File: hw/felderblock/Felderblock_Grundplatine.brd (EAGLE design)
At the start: 100 x 78 mm, 52 parts, among them IC2 LM2936, IC3 ULN2803, IC4 MCP2300X/P, J1 RJ11, J2 RJ11, M1 ARDUINO-NANO-3.0, T2 BC337, X1 TASTENSPERRE1, X2 TASTENSPERRE2, X3 SCHLUESSELSPERRE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

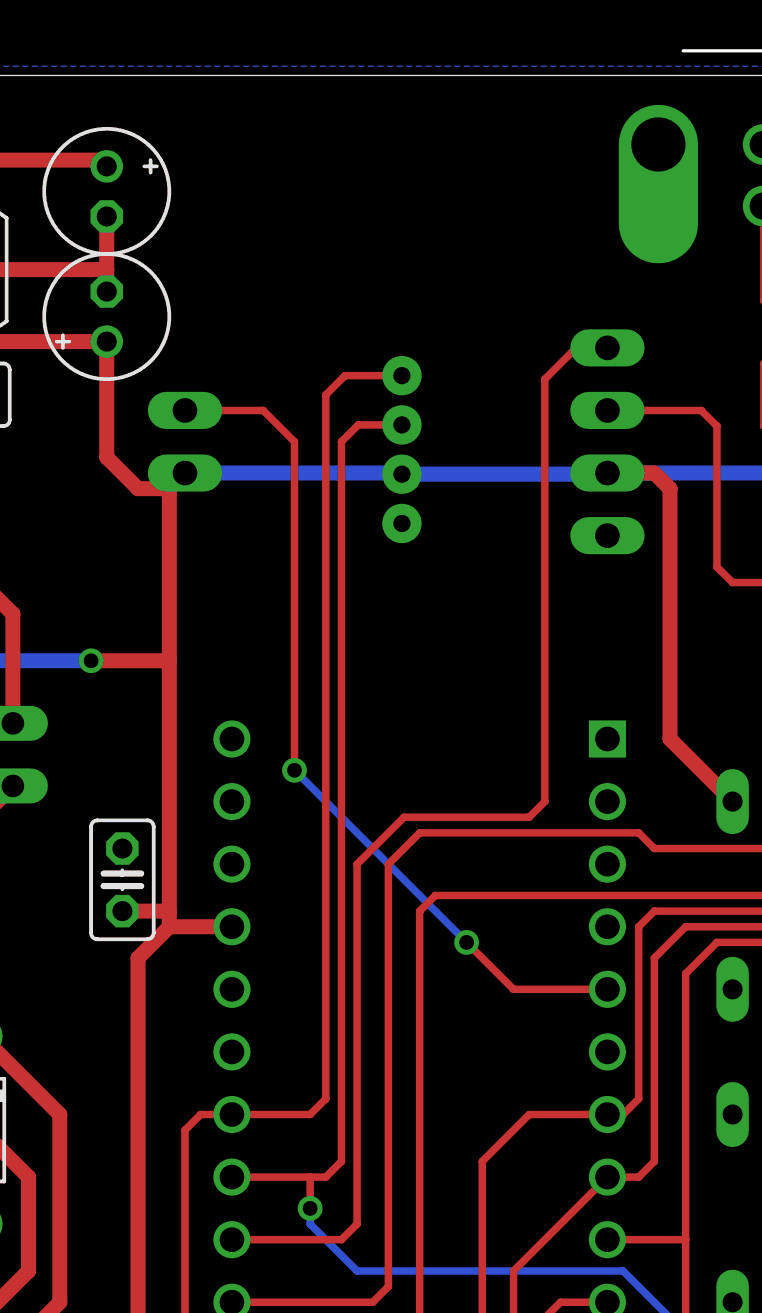
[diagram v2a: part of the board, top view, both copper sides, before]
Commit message: I2c moved
So as not to interfere with other cables. other cables go up, i2c goes down to daughterboard
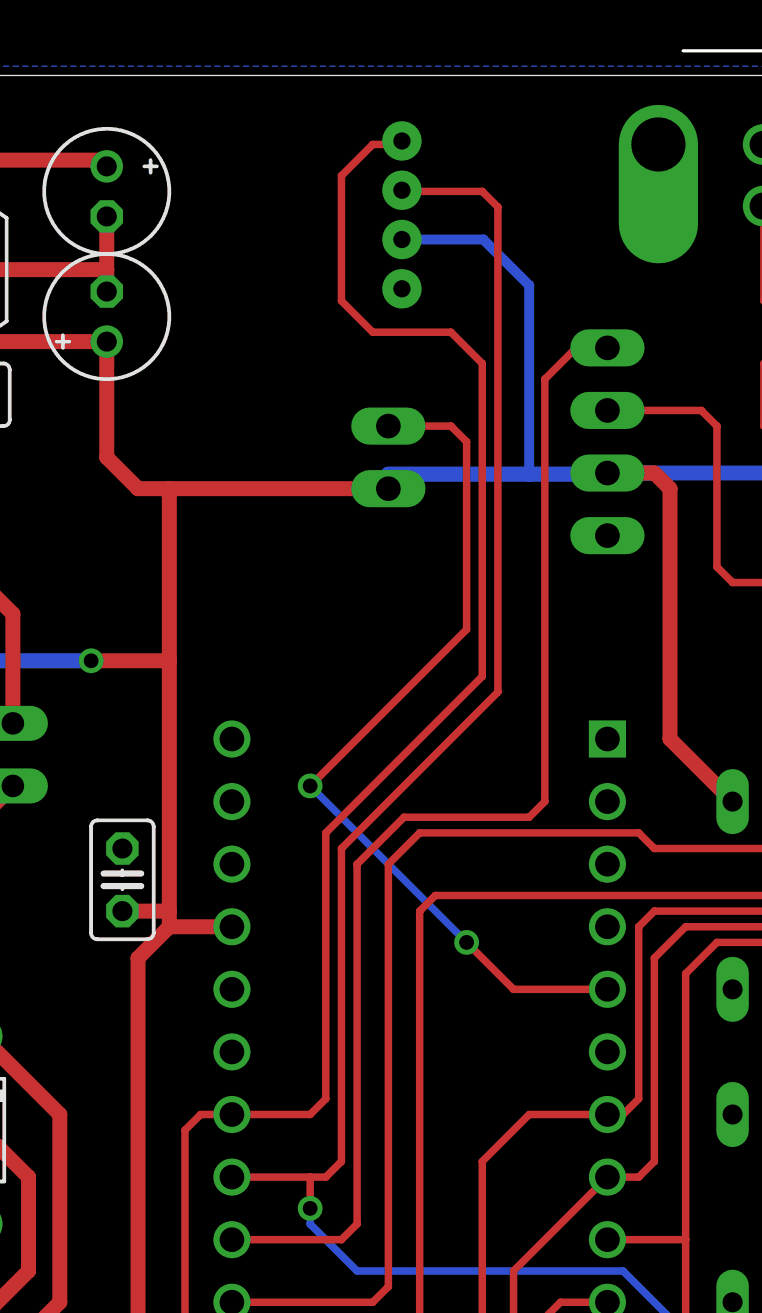
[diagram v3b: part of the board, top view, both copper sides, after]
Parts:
- X3: value SCHLUESSELSPERRE -> SCHL-SPERRE
- moved I2C 9.52 mm to (34.3, 73.3)
- moved X3 8.28 mm to (34.3, 63.5)
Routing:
- net SCL: track 96.9 -> 112.3 mm
- net +5V: track 322.5 -> 336.4 mm, vias 5 -> 4
- net SDA: track 77.6 -> 91.2 mm
- net SCHL_SPERRE: track 34.7 -> 35.5 mm
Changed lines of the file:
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@@
 <?xml version="1.0" encoding="utf-8"?>
 <!DOCTYPE eagle SYSTEM "eagle.dtd">
-<eagle version="7.7.0">
+<eagle version="7.6.0">
 <drawing>
 <settings>
@@
 <attribute name="VALUE" x="13.97" y="67.691" size="1.27" layer="27" ratio="10" rot="R90"/>
 </element>
-<element name="J1" library="SparkFun-Connectors" package="RJ11-6" value="RJ11" x="5.08" y="21.59" rot="MR90">
+<element name="J1" library="SparkFun-Connectors" package="RJ11-6" value="RJ11" x="5.08" y="21.59" smashed="yes" rot="MR90">
 <attribute name="PROD_ID" value="CONN-08590" x="5.08" y="21.59" size="1.778" layer="28" rot="MR90" display="off"/>
 <attribute name="SF_ID" value="PRT-00132" x="5.08" y="21.59" size="1.778" layer="28" rot="MR90" display="off"/>
 </element>
-<element name="J2" library="SparkFun-Connectors" package="RJ11-6" value="RJ11" x="5.08" y="36.83" rot="MR90">
+<element name="J2" library="SparkFun-Connectors" package="RJ11-6" value="RJ11" x="5.08" y="36.83" smashed="yes" rot="MR90">
 <attribute name="PROD_ID" value="CONN-08590" x="5.08" y="36.83" size="1.778" layer="28" rot="MR90" display="off"/>
 <attribute name="SF_ID" value="PRT-00132" x="5.08" y="36.83" size="1.778" layer="28" rot="MR90" display="off"/>
@@
 <attribute name="VALUE" x="55.88" y="58.42" size="1.016" layer="28" ratio="10" rot="MR90"/>
 </element>
-<element name="X3" library="con-molex" package="22-23-2021" value="SCHLUESSELSPERRE" x="26.035" y="64.135" smashed="yes" rot="MR90">
-<attribute name="MF" value="MOLEX" x="26.035" y="64.135" size="1.778" layer="28" rot="MR90" display="off"/>
-<attribute name="OC_NEWARK" value="25C3832" x="26.035" y="64.135" size="1.778" layer="28" rot="MR90" display="off"/>
-<attribute name="MPN" value="22-23-2021" x="26.035" y="64.135" size="1.778" layer="28" rot="MR90" display="off"/>
-<attribute name="OC_FARNELL" value="1462926" x="26.035" y="64.135" size="1.778" layer="28" rot="MR90" display="off"/>
-<attribute name="VALUE" x="29.845" y="57.785" size="1.016" layer="28" ratio="10" rot="MR90"/>
+<element name="X3" library="con-molex" package="22-23-2021" value="SCHL-SPERRE" x="34.29" y="63.5" smashed="yes" rot="MR90">
+<attribute name="MF" value="MOLEX" x="34.29" y="63.5" size="1.778" layer="28" rot="MR90" display="off"/>
+<attribute name="OC_NEWARK" value="25C3832" x="34.29" y="63.5" size="1.778" layer="28" rot="MR90" display="off"/>
+<attribute name="MPN" value="22-23-2021" x="34.29" y="63.5" size="1.778" layer="28" rot="MR90" display="off"/>
+<attribute name="OC_FARNELL" value="1462926" x="34.29" y="63.5" size="1.778" layer="28" rot="MR90" display="off"/>
+<attribute name="VALUE" x="39.37" y="68.58" size="1.016" layer="28" ratio="10" rot="MR270"/>
 </element>
 <element name="IC3" library="uln-udn" package="DIL18" value="ULN2803" x="58.42" y="45.72" smashed="yes" rot="MR0">
@@
 <attribute name="VALUE" x="28.321" y="12.319" size="1.27" layer="27" ratio="10" rot="R180"/>
 </element>
-<element name="I2C" library="SparkFun-Connectors" package="JST-4-PTH-VERT" value="" x="34.29" y="63.8175" rot="MR270">
-<attribute name="PROD_ID" value="CONN-13251" x="34.29" y="63.8175" size="1.778" layer="28" rot="MR270" display="off"/>
+<element name="I2C" library="SparkFun-Connectors" package="JST-4-PTH-VERT" value="" x="34.29" y="73.3425" smashed="yes" rot="MR270">
+<attribute name="PROD_ID" value="CONN-13251" x="34.29" y="73.3425" size="1.778" layer="28" rot="MR270" display="off"/>
+<attribute name="NAME" x="38.735" y="74.4855" size="1.016" layer="26" ratio="20" rot="MR270"/>
+<attribute name="VALUE" x="37.592" y="74.9935" size="0.6096" layer="28" font="vector" ratio="20" rot="MR270"/>
 </element>
 </elements>
@@
 <wire x1="25.4" y1="45.085" x2="25.4" y2="55.245" width="0.6096" layer="1"/>
 <wire x1="25.4" y1="55.245" x2="25.4" y2="62.23" width="0.6096" layer="1"/>
-<wire x1="25.4" y1="62.23" x2="26.035" y2="62.865" width="0.6096" layer="1"/>
 <wire x1="24.13" y1="43.18" x2="24.13" y2="14.605" width="0.6096" layer="1"/>
 <wire x1="24.13" y1="14.605" x2="26.67" y2="12.065" width="0.6096" layer="1"/>
@@
 <wire x1="97.155" y1="8.89" x2="93.345" y2="8.89" width="0.3048" layer="1"/>
 <contactref element="I2C" pad="3"/>
-<wire x1="26.035" y1="62.8175" x2="26.035" y2="62.865" width="0.6096" layer="16"/>
-<via x="26.035" y="62.8175" extent="1-16" drill="0.6" shape="square"/>
 <wire x1="43.18" y1="62.865" x2="43.1325" y2="62.8175" width="0.6096" layer="16"/>
-<wire x1="43.1325" y1="62.8175" x2="34.84" y2="62.8175" width="0.6096" layer="16"/>
-<wire x1="34.84" y1="62.8175" x2="34.7925" y2="62.865" width="0.6096" layer="16"/>
-<wire x1="34.7925" y1="62.865" x2="26.035" y2="62.865" width="0.6096" layer="16"/>
+<wire x1="25.4" y1="62.23" x2="34.29" y2="62.23" width="0.6096" layer="1"/>
+<wire x1="43.1325" y1="62.8175" x2="40.005" y2="62.8175" width="0.6096" layer="16"/>
+<wire x1="40.005" y1="62.8175" x2="34.29" y2="62.8175" width="0.6096" layer="16"/>
+<wire x1="34.29" y1="62.8175" x2="34.29" y2="62.23" width="0.6096" layer="16"/>
+<wire x1="34.84" y1="72.3425" x2="38.1475" y2="72.3425" width="0.4064" layer="16"/>
+<wire x1="38.1475" y1="72.3425" x2="40.005" y2="70.485" width="0.4064" layer="16"/>
+<wire x1="40.005" y1="70.485" x2="40.005" y2="62.8175" width="0.4064" layer="16"/>
 </signal>
 <signal name="LN_TX">
@@
 <wire x1="43.815" y1="30.48" x2="47.625" y2="26.67" width="0.3048" layer="16"/>
 <contactref element="I2C" pad="2"/>
-<wire x1="32.385" y1="34.925" x2="32.385" y2="64.135" width="0.3048" layer="1"/>
-<wire x1="32.385" y1="64.135" x2="33.0675" y2="64.8175" width="0.3048" layer="1"/>
-<wire x1="33.0675" y1="64.8175" x2="34.84" y2="64.8175" width="0.3048" layer="1"/>
+<wire x1="32.385" y1="34.925" x2="32.385" y2="47.625" width="0.3048" layer="1"/>
+<wire x1="32.385" y1="47.625" x2="38.735" y2="53.975" width="0.3048" layer="1"/>
+<wire x1="38.735" y1="53.975" x2="38.735" y2="73.66" width="0.3048" layer="1"/>
+<wire x1="38.735" y1="73.66" x2="38.1" y2="74.295" width="0.3048" layer="1"/>
+<wire x1="38.1" y1="74.295" x2="34.8875" y2="74.295" width="0.3048" layer="1"/>
+<wire x1="34.8875" y1="74.295" x2="34.84" y2="74.3425" width="0.3048" layer="1"/>
 </signal>
 <signal name="SCL">
 <contactref element="M1" pad="J2.7"/>
-<wire x1="31.75" y1="66.04" x2="31.75" y2="37.465" width="0.3048" layer="1"/>
 <wire x1="31.75" y1="37.465" x2="31.115" y2="36.83" width="0.3048" layer="1"/>
 <wire x1="31.115" y1="36.83" x2="27.94" y2="36.83" width="0.3048" layer="1"/>
@@
 <wire x1="68.58" y1="26.67" x2="68.58" y2="29.21" width="0.3048" layer="1"/>
 <contactref element="I2C" pad="1"/>
-<wire x1="31.75" y1="66.04" x2="32.5275" y2="66.8175" width="0.3048" layer="1"/>
-<wire x1="32.5275" y1="66.8175" x2="34.84" y2="66.8175" width="0.3048" layer="1"/>
+<wire x1="31.75" y1="37.465" x2="31.75" y2="48.26" width="0.3048" layer="1"/>
+<wire x1="31.75" y1="48.26" x2="38.1" y2="54.61" width="0.3048" layer="1"/>
+<wire x1="38.1" y1="54.61" x2="38.1" y2="67.31" width="0.3048" layer="1"/>
+<wire x1="38.1" y1="67.31" x2="36.83" y2="68.58" width="0.3048" layer="1"/>
+<wire x1="36.83" y1="68.58" x2="33.655" y2="68.58" width="0.3048" layer="1"/>
+<wire x1="33.655" y1="68.58" x2="32.385" y2="69.85" width="0.3048" layer="1"/>
+<wire x1="32.385" y1="69.85" x2="32.385" y2="74.93" width="0.3048" layer="1"/>
+<wire x1="32.385" y1="74.93" x2="33.655" y2="76.2" width="0.3048" layer="1"/>
+<wire x1="33.655" y1="76.2" x2="34.6975" y2="76.2" width="0.3048" layer="1"/>
+<wire x1="34.6975" y1="76.2" x2="34.84" y2="76.3425" width="0.3048" layer="1"/>
 </signal>
 <signal name="FELD3_LED">
@@
 <wire x1="39.37" y1="41.91" x2="37.465" y2="43.815" width="0.3048" layer="1"/>
 <via x="37.465" y="43.815" extent="1-16" drill="0.6" shape="square"/>
-<wire x1="37.465" y1="43.815" x2="30.48" y2="50.8" width="0.3048" layer="16"/>
-<via x="30.48" y="50.8" extent="1-16" drill="0.6" shape="square"/>
-<wire x1="30.48" y1="50.8" x2="30.48" y2="64.135" width="0.3048" layer="1"/>
-<wire x1="30.48" y1="64.135" x2="29.21" y2="65.405" width="0.3048" layer="1"/>
-<wire x1="29.21" y1="65.405" x2="26.035" y2="65.405" width="0.3048" layer="1"/>
+<wire x1="37.465" y1="43.815" x2="31.115" y2="50.165" width="0.3048" layer="16"/>
+<via x="31.115" y="50.165" extent="1-16" drill="0.6" shape="square"/>
+<wire x1="31.115" y1="50.165" x2="37.465" y2="56.515" width="0.3048" layer="1"/>
+<wire x1="37.465" y1="56.515" x2="37.465" y2="64.135" width="0.3048" layer="1"/>
+<wire x1="37.465" y1="64.135" x2="36.83" y2="64.77" width="0.3048" layer="1"/>
+<wire x1="36.83" y1="64.77" x2="34.29" y2="64.77" width="0.3048" layer="1"/>
 </signal>
 <signal name="TSP1_LED">

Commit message: some tuning
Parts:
- flipped C4 to the bottom
- flipped C5 to the bottom
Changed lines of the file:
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@@
 <attribute name="VALUE" x="26.289" y="44.069" size="1.27" layer="27" ratio="10" rot="R90"/>
 </element>
-<element name="C4" library="resistor" package="E2-5" value="10uF" x="22.86" y="74.295" smashed="yes" rot="R270">
-<attribute name="VALUE" x="25.781" y="69.85" size="1.27" layer="27" ratio="10" rot="R270"/>
-</element>
-<element name="C5" library="resistor" package="E2-5" value="10uF" x="22.86" y="69.215" smashed="yes" rot="R90">
-<attribute name="VALUE" x="26.924" y="73.66" size="1.27" layer="27" ratio="10" rot="R90"/>
+<element name="C4" library="resistor" package="E2-5" value="10uF" x="22.86" y="74.295" smashed="yes" rot="MR270">
+<attribute name="VALUE" x="19.939" y="69.85" size="1.27" layer="28" ratio="10" rot="MR270"/>
+</element>
+<element name="C5" library="resistor" package="E2-5" value="10uF" x="22.86" y="69.215" smashed="yes" rot="MR90">
+<attribute name="VALUE" x="18.796" y="73.66" size="1.27" layer="28" ratio="10" rot="MR90"/>
 </element>
 <element name="D1" library="diode" package="DO41-7.6" value="1N5819-T" x="17.78" y="21.59" smashed="yes" rot="R270">
@@
 <contactref element="IC4" pad="6"/>
 <contactref element="IC4" pad="8"/>
-<wire x1="22.86" y1="70.231" x2="22.86" y2="71.12" width="0.6096" layer="1"/>
-<wire x1="22.86" y1="71.12" x2="22.86" y2="73.279" width="0.6096" layer="1"/>
 <wire x1="15.24" y1="71.12" x2="22.86" y2="71.12" width="0.6096" layer="1"/>
 <contactref element="I2C" pad="4"/>
+<wire x1="22.86" y1="70.231" x2="22.86" y2="73.279" width="0.6096" layer="1"/>
 </signal>
 <signal name="LOCONET">
@@
 <wire x1="25.4" y1="62.23" x2="24.13" y2="62.23" width="0.6096" layer="1"/>
 <wire x1="24.13" y1="62.23" x2="22.86" y2="63.5" width="0.6096" layer="1"/>
-<wire x1="22.86" y1="63.5" x2="22.86" y2="68.199" width="0.6096" layer="1"/>
-<wire x1="17.145" y1="69.85" x2="17.145" y2="67.945" width="0.6096" layer="1"/>
-<wire x1="17.145" y1="67.945" x2="17.145" y2="66.675" width="0.6096" layer="1"/>
-<wire x1="17.145" y1="66.675" x2="17.78" y2="66.04" width="0.6096" layer="1"/>
-<wire x1="22.86" y1="68.199" x2="17.399" y2="68.199" width="0.6096" layer="1"/>
-<wire x1="17.399" y1="68.199" x2="17.145" y2="67.945" width="0.6096" layer="1"/>
 <wire x1="24.13" y1="43.18" x2="25.4" y2="44.45" width="0.6096" layer="1"/>
 <wire x1="23.495" y1="45.085" x2="25.4" y2="45.085" width="0.6096" layer="1"/>
@@
 <wire x1="38.1475" y1="72.3425" x2="40.005" y2="70.485" width="0.4064" layer="16"/>
 <wire x1="40.005" y1="70.485" x2="40.005" y2="62.8175" width="0.4064" layer="16"/>
+<wire x1="22.86" y1="63.5" x2="22.86" y2="68.199" width="0.6096" layer="1"/>
+<wire x1="17.145" y1="69.85" x2="17.78" y2="69.85" width="0.6096" layer="1"/>
+<wire x1="17.78" y1="69.85" x2="17.78" y2="68.199" width="0.6096" layer="1"/>
+<wire x1="17.78" y1="67.945" x2="17.78" y2="66.04" width="0.6096" layer="1"/>
+<wire x1="22.86" y1="68.199" x2="17.78" y2="68.199" width="0.6096" layer="1"/>
+<wire x1="17.78" y1="68.199" x2="17.78" y2="67.945" width="0.6096" layer="1"/>
 </signal>
 <signal name="LN_TX">
@@
 <contactref element="IC2" pad="3"/>
 <contactref element="C4" pad="+"/>
-<wire x1="17.145" y1="75.565" x2="22.606" y2="75.565" width="0.6096" layer="1"/>
-<wire x1="22.606" y1="75.565" x2="22.86" y2="75.311" width="0.6096" layer="1"/>
 <wire x1="17.145" y1="75.565" x2="17.145" y2="72.39" width="0.6096" layer="1"/>
 <wire x1="19.05" y1="57.15" x2="13.335" y2="62.865" width="0.6096" layer="1"/>
@@
 <wire x1="15.875" y1="73.025" x2="17.145" y2="72.39" width="0.6096" layer="1"/>
 <wire x1="19.05" y1="52.705" x2="19.05" y2="57.15" width="0.6096" layer="1"/>
+<wire x1="17.145" y1="75.565" x2="22.86" y2="75.565" width="0.6096" layer="1"/>
+<wire x1="22.86" y1="75.565" x2="22.86" y2="75.311" width="0.6096" layer="1"/>
 </signal>
 <signal name="RS2">

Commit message: last update for mfg
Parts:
- added R1, R2: 4K7, resistor:0207/7
- moved C3 1.42 mm to (24.8, 45.7)
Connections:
- net +5V: now also R1.2, R2.2
- net SCL: now also R1.1
- net SDA: now also R2.1
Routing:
- net +5V: track 336.0 -> 341.5 mm
- net SDA: track 91.2 -> 95.5 mm
- net SCL: track 112.3 -> 113.5 mm
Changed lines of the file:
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@@
 <attribute name="VALUE" x="18.796" y="64.389" size="1.27" layer="27" ratio="10" rot="R180"/>
 </element>
-<element name="C3" library="resistor" package="C025-025X050" value="100nF" x="23.495" y="46.355" smashed="yes" rot="R90">
-<attribute name="VALUE" x="26.289" y="44.069" size="1.27" layer="27" ratio="10" rot="R90"/>
+<element name="C3" library="resistor" package="C025-025X050" value="100nF" x="24.765" y="45.72" smashed="yes" rot="R90">
+<attribute name="VALUE" x="27.559" y="43.434" size="1.27" layer="27" ratio="10" rot="R90"/>
 </element>
 <element name="C4" library="resistor" package="E2-5" value="10uF" x="22.86" y="74.295" smashed="yes" rot="MR270">
@@
 <attribute name="VALUE" x="37.592" y="74.9935" size="0.6096" layer="28" font="vector" ratio="20" rot="MR270"/>
 </element>
+<element name="R1" library="resistor" package="0207/7" value="4K7" x="24.765" y="37.465" rot="R90"/>
+<element name="R2" library="resistor" package="0207/7" value="4K7" x="24.765" y="27.94" rot="R270"/>
 </elements>
 <signals>
@@
 <wire x1="52.07" y1="62.865" x2="43.18" y2="62.865" width="0.6096" layer="16"/>
 <contactref element="IC4" pad="18"/>
-<wire x1="27.94" y1="44.45" x2="25.4" y2="44.45" width="0.6096" layer="1"/>
-<wire x1="25.4" y1="44.45" x2="25.4" y2="45.085" width="0.6096" layer="1"/>
-<wire x1="25.4" y1="45.085" x2="25.4" y2="55.245" width="0.6096" layer="1"/>
 <wire x1="25.4" y1="55.245" x2="25.4" y2="62.23" width="0.6096" layer="1"/>
-<wire x1="24.13" y1="43.18" x2="24.13" y2="14.605" width="0.6096" layer="1"/>
-<wire x1="24.13" y1="14.605" x2="26.67" y2="12.065" width="0.6096" layer="1"/>
+<wire x1="22.86" y1="15.875" x2="26.67" y2="12.065" width="0.6096" layer="1"/>
 <wire x1="26.67" y1="12.065" x2="36.83" y2="12.065" width="0.6096" layer="1"/>
 <via x="36.83" y="12.065" extent="1-16" drill="0.6" shape="square"/>
@@
 <wire x1="25.4" y1="62.23" x2="24.13" y2="62.23" width="0.6096" layer="1"/>
 <wire x1="24.13" y1="62.23" x2="22.86" y2="63.5" width="0.6096" layer="1"/>
-<wire x1="24.13" y1="43.18" x2="25.4" y2="44.45" width="0.6096" layer="1"/>
-<wire x1="23.495" y1="45.085" x2="25.4" y2="45.085" width="0.6096" layer="1"/>
 <wire x1="16.51" y1="55.245" x2="22.225" y2="55.245" width="0.6096" layer="16"/>
 <via x="22.225" y="55.245" extent="1-16" drill="0.6" shape="square"/>
@@
 <wire x1="17.145" y1="69.85" x2="17.78" y2="69.85" width="0.6096" layer="1"/>
 <wire x1="17.78" y1="69.85" x2="17.78" y2="68.199" width="0.6096" layer="1"/>
-<wire x1="17.78" y1="67.945" x2="17.78" y2="66.04" width="0.6096" layer="1"/>
+<wire x1="17.78" y1="68.199" x2="17.78" y2="66.04" width="0.6096" layer="1"/>
 <wire x1="22.86" y1="68.199" x2="17.78" y2="68.199" width="0.6096" layer="1"/>
-<wire x1="17.78" y1="68.199" x2="17.78" y2="67.945" width="0.6096" layer="1"/>
+<contactref element="R2" pad="2"/>
+<contactref element="R1" pad="2"/>
+<wire x1="22.86" y1="15.875" x2="22.86" y2="24.13" width="0.6096" layer="1"/>
+<wire x1="22.86" y1="24.13" x2="22.86" y2="41.275" width="0.6096" layer="1"/>
+<wire x1="22.86" y1="41.275" x2="22.86" y2="44.45" width="0.6096" layer="1"/>
+<wire x1="22.86" y1="44.45" x2="22.86" y2="52.705" width="0.6096" layer="1"/>
+<wire x1="22.86" y1="52.705" x2="25.4" y2="55.245" width="0.6096" layer="1"/>
+<wire x1="27.94" y1="44.45" x2="24.765" y2="44.45" width="0.6096" layer="1"/>
+<wire x1="24.765" y1="44.45" x2="22.86" y2="44.45" width="0.6096" layer="1"/>
+<wire x1="24.765" y1="41.275" x2="22.86" y2="41.275" width="0.3048" layer="1"/>
+<wire x1="24.765" y1="24.13" x2="22.86" y2="24.13" width="0.3048" layer="1"/>
 </signal>
 <signal name="LN_TX">
@@
 <wire x1="38.1" y1="74.295" x2="34.8875" y2="74.295" width="0.3048" layer="1"/>
 <wire x1="34.8875" y1="74.295" x2="34.84" y2="74.3425" width="0.3048" layer="1"/>
+<contactref element="R2" pad="1"/>
+<wire x1="27.94" y1="34.29" x2="27.305" y2="34.29" width="0.3048" layer="16"/>
+<wire x1="27.305" y1="34.29" x2="24.765" y2="31.75" width="0.3048" layer="16"/>
 </signal>
 <signal name="SCL">
@@
 <wire x1="34.29" y1="25.4" x2="26.67" y2="25.4" width="0.3048" layer="1"/>
 <wire x1="26.67" y1="25.4" x2="26.035" y2="26.035" width="0.3048" layer="1"/>
-<wire x1="26.035" y1="26.035" x2="26.035" y2="36.195" width="0.3048" layer="1"/>
+<wire x1="26.035" y1="26.035" x2="26.035" y2="33.655" width="0.3048" layer="1"/>
+<wire x1="26.035" y1="33.655" x2="26.035" y2="36.195" width="0.3048" layer="1"/>
 <wire x1="26.035" y1="36.195" x2="26.67" y2="36.83" width="0.3048" layer="1"/>
 <wire x1="26.67" y1="36.83" x2="27.94" y2="36.83" width="0.3048" layer="1"/>
@@
 <wire x1="33.655" y1="76.2" x2="34.6975" y2="76.2" width="0.3048" layer="1"/>
 <wire x1="34.6975" y1="76.2" x2="34.84" y2="76.3425" width="0.3048" layer="1"/>
+<contactref element="R1" pad="1"/>
+<wire x1="24.765" y1="33.655" x2="26.035" y2="33.655" width="0.3048" layer="1"/>
 </signal>
 <signal name="FELD3_LED">
